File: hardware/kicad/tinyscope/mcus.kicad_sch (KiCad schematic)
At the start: 14 parts, among them U10 STM32H753VITx

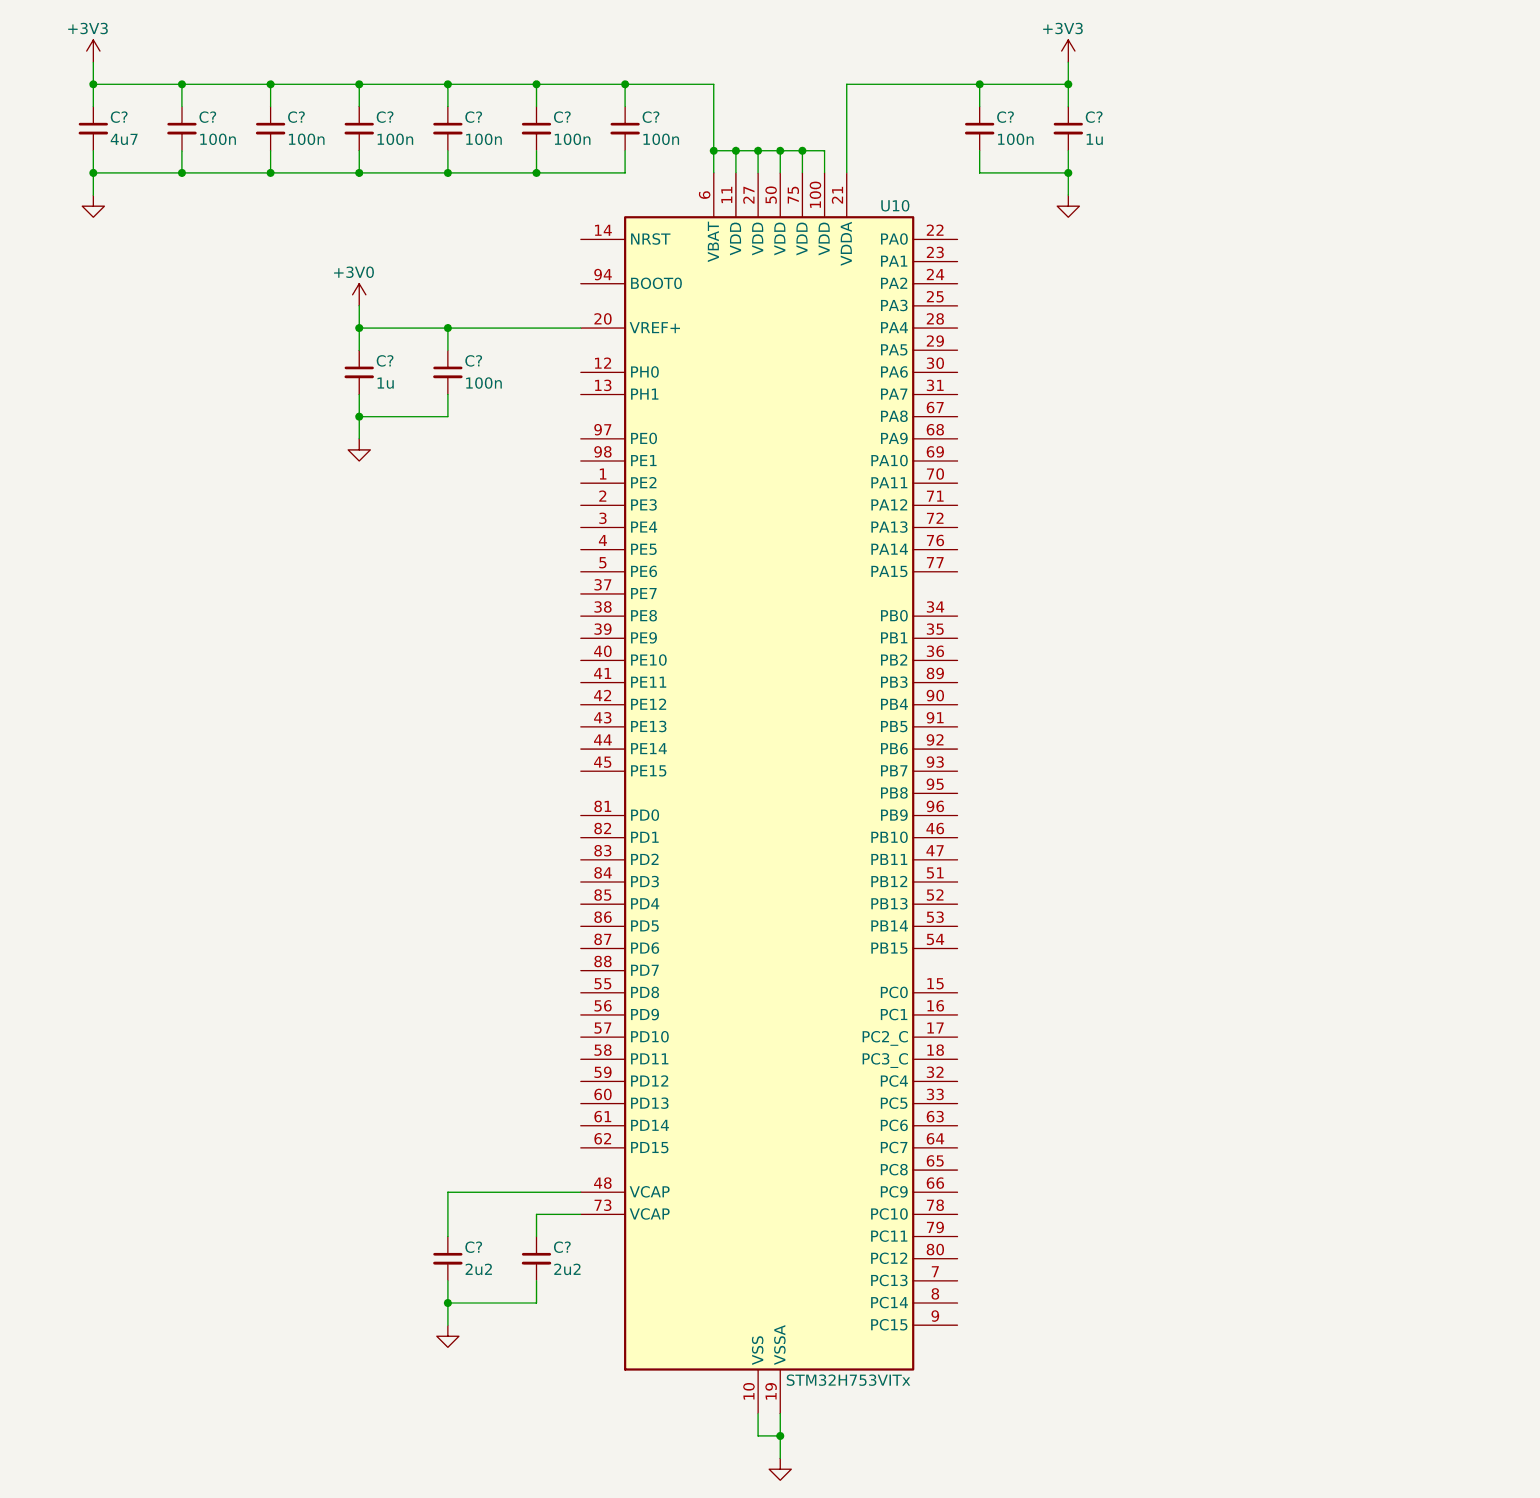
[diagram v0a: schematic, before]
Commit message: feat: hardware: Add tinyscope kicad project. Adds SWD NRST and BOOT0
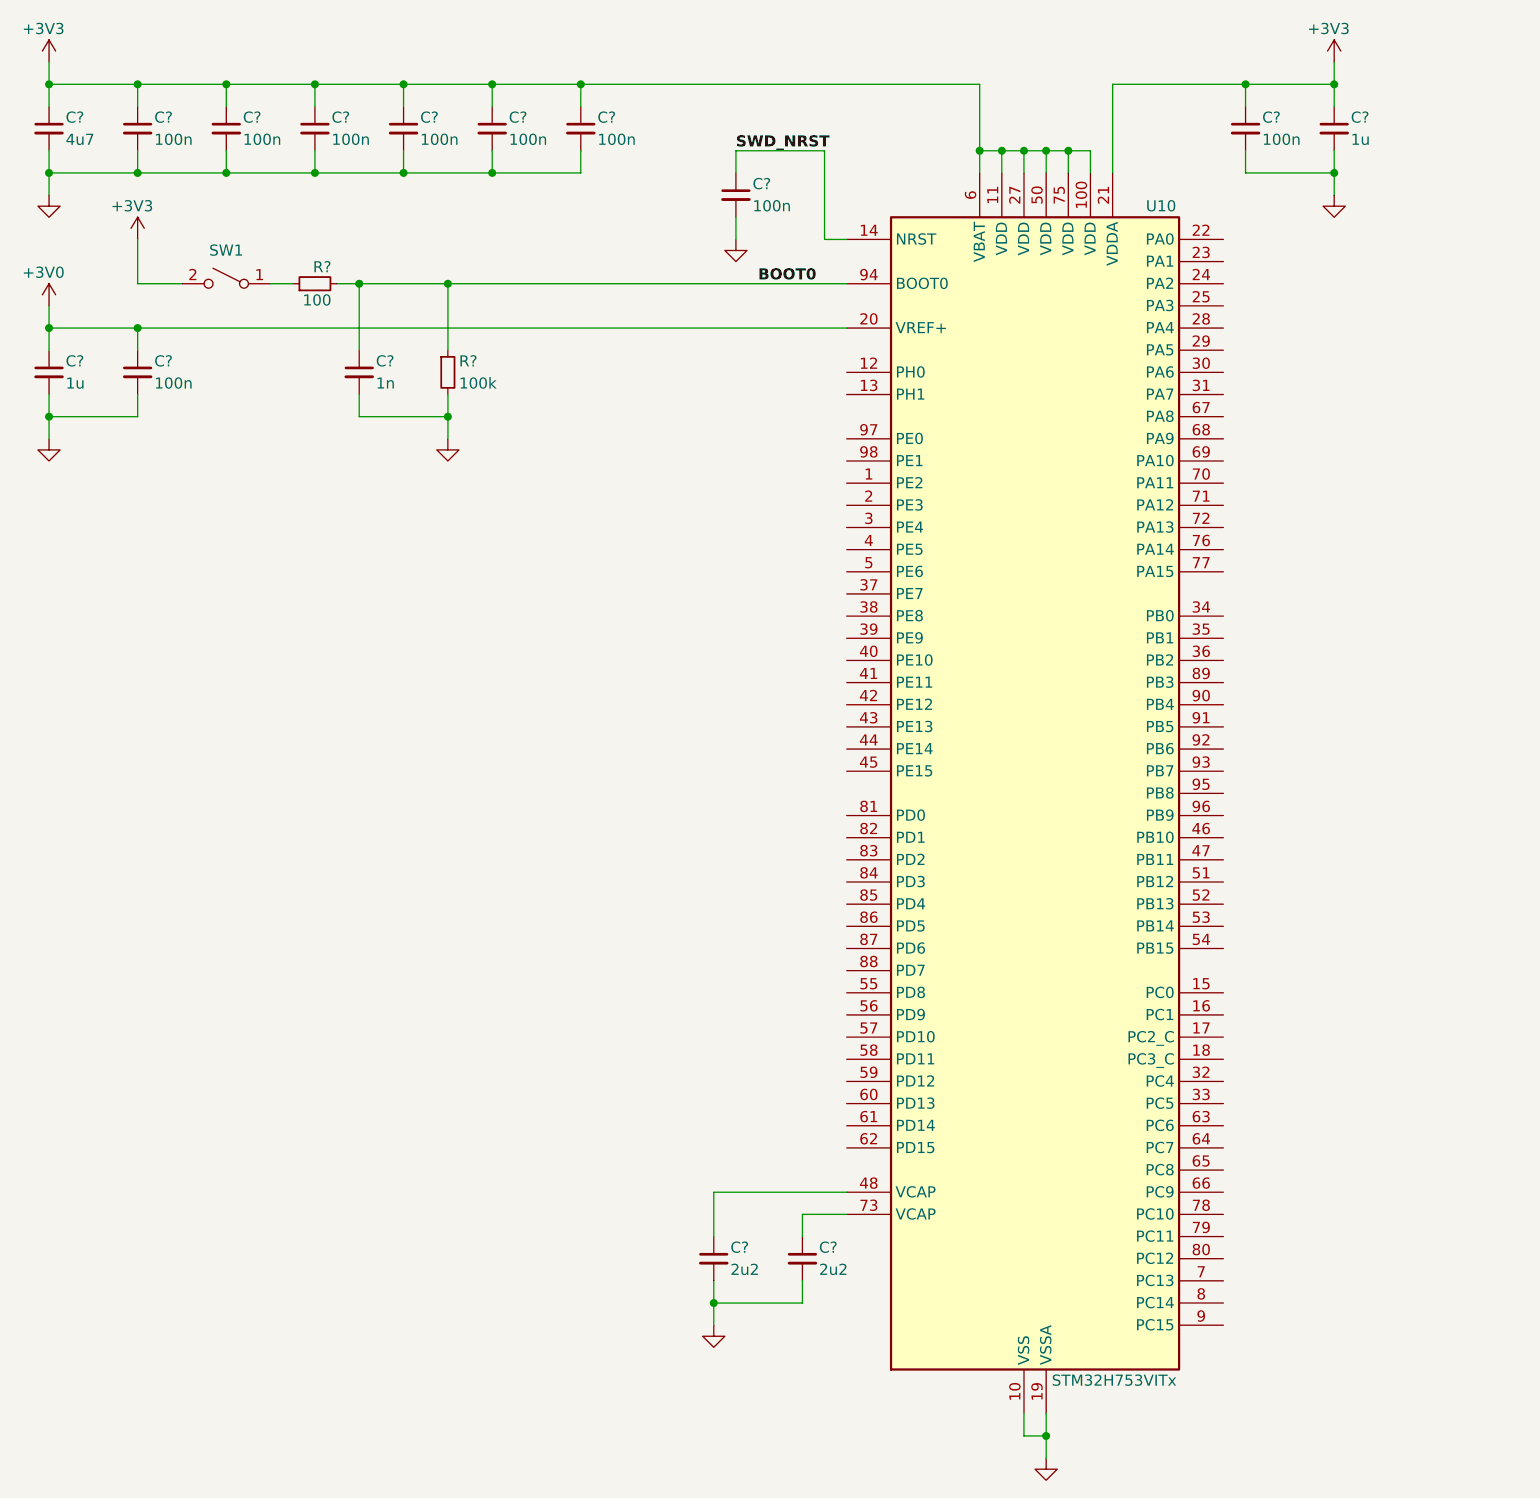
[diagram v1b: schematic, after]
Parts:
- added C?: 100n, symbol Device:C_Small
- added C?: 1n, symbol Device:C_Small
- added R?: 100k, symbol Device:R_Small
- added R?: 100, symbol Device:R_Small
- added SW1: SW_SPST, symbol Switch:SW_SPST
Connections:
- net +3V3: now also SW1.2 (B)
- net GND: now also C?.2, C?.2, R?.2
- net SWD_NRST: now reaches U10.14 (NRST)
- net SWD_NRST: now also C?.1
- net BOOT0: now reaches U10.94 (BOOT0)
- net BOOT0: now also C?.1, R?.1, R?.2
- new net: R?.1, SW1.1 (A)
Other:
- moved on the sheet: C?, U10

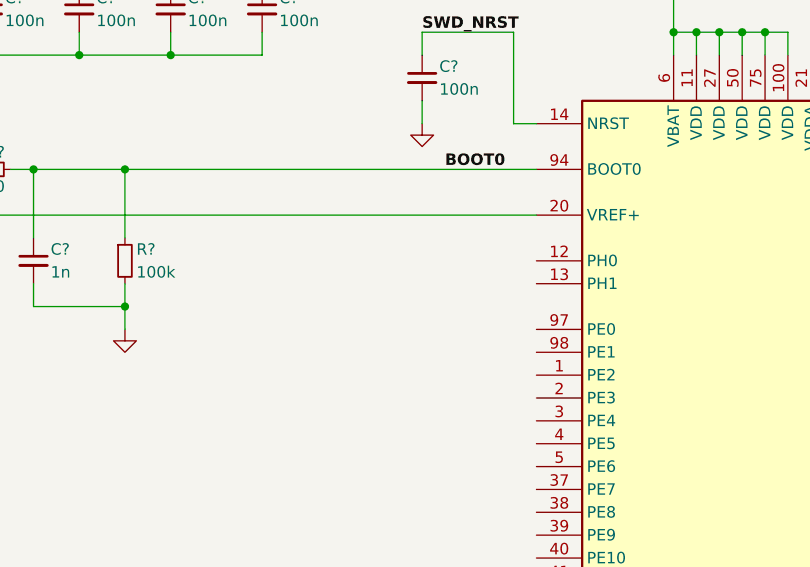
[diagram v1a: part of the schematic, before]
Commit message: feat: hardware: Add tinyscope kicad project. Adds HSE XTAL. Missing capacitor values
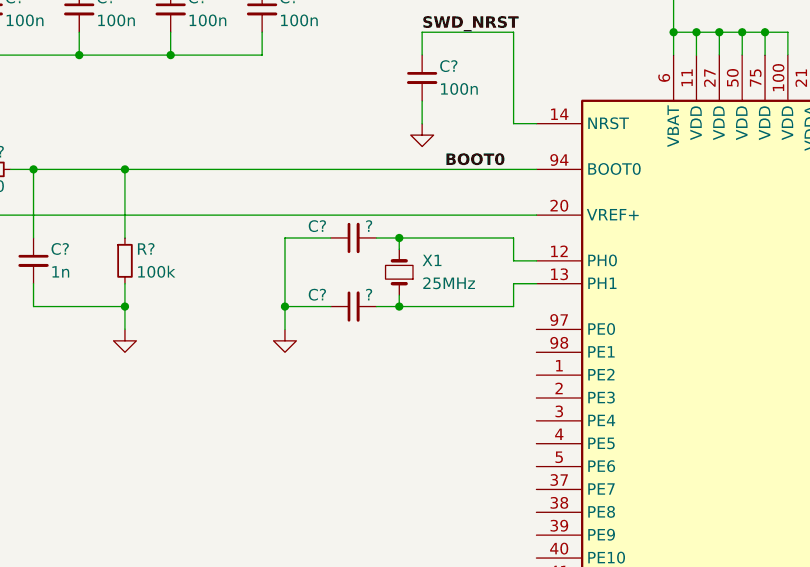
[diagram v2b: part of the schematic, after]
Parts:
- added C? (x2): ?, symbol Device:C_Small
- added X1: 25MHz, symbol Device:Crystal_Small
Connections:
- net GND: now also C?.1, C?.1
- net at U10.12 (PH0): now also C?.2, X1.2
- net at U10.13 (PH1): now also C?.2, X1.1
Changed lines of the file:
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@@
 (kicad_sch (version 20230121) (generator eeschema)
   (paper "A4")
+  (junction (at 96.52 60.96) (diameter 0) (color 0 0 0 0)
+  )
+  (junction (at 83.82 60.96) (diameter 0) (color 0 0 0 0)
+  )
   (junction (at 50.8 33.02) (diameter 0) (color 0 0 0 0)
   )
@@
   (junction (at 40.64 22.86) (diameter 0) (color 0 0 0 0)
   )
+  (junction (at 96.52 53.34) (diameter 0) (color 0 0 0 0)
+  )
   (junction (at 66.04 45.72) (diameter 0) (color 0 0 0 0)
   )
@@
     (stroke (width 0) (type default))
   )
+  (wire (pts (xy 109.22 58.42) (xy 109.22 60.96))
+    (stroke (width 0) (type default))
+  )
   (wire (pts (xy 167.64 33.02) (xy 167.64 35.56))
     (stroke (width 0) (type default))
@@
     (stroke (width 0) (type default))
   )
+  (wire (pts (xy 83.82 60.96) (xy 83.82 63.5))
+    (stroke (width 0) (type default))
+  )
   (wire (pts (xy 50.8 33.02) (xy 40.64 33.02))
     (stroke (width 0) (type default))
@@
     (stroke (width 0) (type default))
   )
+  (wire (pts (xy 111.76 55.88) (xy 109.22 55.88))
+    (stroke (width 0) (type default))
+  )
+  (wire (pts (xy 96.52 60.96) (xy 109.22 60.96))
+    (stroke (width 0) (type default))
+  )
   (wire (pts (xy 30.48 33.02) (xy 30.48 30.48))
     (stroke (width 0) (type default))
@@
     (stroke (width 0) (type default))
   )
+  (wire (pts (xy 109.22 55.88) (xy 109.22 53.34))
+    (stroke (width 0) (type default))
+  )
+  (wire (pts (xy 83.82 53.34) (xy 83.82 60.96))
+    (stroke (width 0) (type default))
+  )
   (wire (pts (xy 20.32 22.86) (xy 30.48 22.86))
     (stroke (width 0) (type default))
@@
     (stroke (width 0) (type default))
   )
+  (wire (pts (xy 93.98 60.96) (xy 96.52 60.96))
+    (stroke (width 0) (type default))
+  )
+  (wire (pts (xy 88.9 53.34) (xy 83.82 53.34))
+    (stroke (width 0) (type default))
+  )
   (wire (pts (xy 55.88 60.96) (xy 66.04 60.96))
     (stroke (width 0) (type default))
   )
+  (wire (pts (xy 93.98 53.34) (xy 96.52 53.34))
+    (stroke (width 0) (type default))
+  )
   (wire (pts (xy 127 30.48) (xy 127 22.86))
     (stroke (width 0) (type default))
@@
     (stroke (width 0) (type default))
   )
+  (wire (pts (xy 96.52 53.34) (xy 96.52 54.61))
+    (stroke (width 0) (type default))
+  )
   (wire (pts (xy 30.48 50.8) (xy 111.76 50.8))
     (stroke (width 0) (type default))
   )
+  (wire (pts (xy 111.76 58.42) (xy 109.22 58.42))
+    (stroke (width 0) (type default))
+  )
   (wire (pts (xy 96.52 162.56) (xy 106.68 162.56))
     (stroke (width 0) (type default))
@@
     (stroke (width 0) (type default))
   )
+  (wire (pts (xy 88.9 60.96) (xy 83.82 60.96))
+    (stroke (width 0) (type default))
+  )
   (wire (pts (xy 81.28 22.86) (xy 71.12 22.86))
     (stroke (width 0) (type default))
@@
     (stroke (width 0) (type default))
   )
+  (wire (pts (xy 96.52 53.34) (xy 109.22 53.34))
+    (stroke (width 0) (type default))
+  )
   (wire (pts (xy 129.54 33.02) (xy 129.54 30.48))
     (stroke (width 0) (type default))
   )
   (wire (pts (xy 81.28 22.86) (xy 81.28 25.4))
+    (stroke (width 0) (type default))
+  )
+  (wire (pts (xy 96.52 59.69) (xy 96.52 60.96))
     (stroke (width 0) (type default))
   )
@@
     )
   )
+  (symbol (lib_id "Device:C_Small") (at 91.44 53.34 90) (mirror x) (unit 1)
+    (in_bom yes) (on_board yes) (dnp no)
+    (property "Reference" "C?" (at 86.36 52.07 90)
+      (effects (font (size 1.27 1.27)) (justify right))
+    )
+    (property "Value" "?" (at 92.71 52.07 90)
+      (effects (font (size 1.27 1.27)) (justify right))
+    )
+    (property "Footprint" "" (at 91.44 53.34 0)
+      (effects (font (size 1.27 1.27)) hide)
+    )
+    (property "Datasheet" "~" (at 91.44 53.34 0)
+      (effects (font (size 1.27 1.27)) hide)
+    )
+    (pin "1")
+    (pin "2")
+    (instances
+      (project "tinyscope"
+        (path "/bb072e32-cc57-415a-8554-0e84d374f333"
+          (reference "C?") (unit 1)
+        )
+        (path "/bb072e32-cc57-415a-8554-0e84d374f333/7c1b1425-60eb-4f71-b125-42ba246f39fb"
+          (reference "C1") (unit 1)
+        )
+        (path "/bb072e32-cc57-415a-8554-0e84d374f333/f3c865ab-23cb-49a1-bb6d-4ee24e55c7fa"
+          (reference "C42") (unit 1)
+        )
+      )
+    )
+  )
   (symbol (lib_id "Device:C_Small") (at 71.12 27.94 0) (mirror y) (unit 1)
     (in_bom yes) (on_board yes) (dnp no)
@@
         (path "/bb072e32-cc57-415a-8554-0e84d374f333/f3c865ab-23cb-49a1-bb6d-4ee24e55c7fa"
           (reference "C27") (unit 1)
+        )
+      )
+    )
+  )
+  (symbol (lib_id "Device:Crystal_Small") (at 96.52 57.15 90) (unit 1)
+    (in_bom yes) (on_board yes) (dnp no) (fields_autoplaced)
+    (property "Reference" "X1" (at 99.06 55.88 90)
+      (effects (font (size 1.27 1.27)) (justify right))
+    )
+    (property "Value" "25MHz" (at 99.06 58.42 90)
+      (effects (font (size 1.27 1.27)) (justify right))
+    )
+    (property "Footprint" "" (at 96.52 57.15 0)
+      (effects (font (size 1.27 1.27)) hide)
+    )
+    (property "Datasheet" "~" (at 96.52 57.15 0)
+      (effects (font (size 1.27 1.27)) hide)
+    )
+    (pin "1")
+    (pin "2")
+    (instances
+      (project "tinyscope"
+        (path "/bb072e32-cc57-415a-8554-0e84d374f333/f3c865ab-23cb-49a1-bb6d-4ee24e55c7fa"
+          (reference "X1") (unit 1)
         )
       )
@@
         (path "/bb072e32-cc57-415a-8554-0e84d374f333/f3c865ab-23cb-49a1-bb6d-4ee24e55c7fa"
           (reference "C35") (unit 1)
+        )
+      )
+    )
+  )
+  (symbol (lib_id "Device:C_Small") (at 91.44 60.96 90) (mirror x) (unit 1)
+    (in_bom yes) (on_board yes) (dnp no)
+    (property "Reference" "C?" (at 86.36 59.69 90)
+      (effects (font (size 1.27 1.27)) (justify right))
+    )
+    (property "Value" "?" (at 92.71 59.69 90)
+      (effects (font (size 1.27 1.27)) (justify right))
+    )
+    (property "Footprint" "" (at 91.44 60.96 0)
+      (effects (font (size 1.27 1.27)) hide)
+    )
+    (property "Datasheet" "~" (at 91.44 60.96 0)
+      (effects (font (size 1.27 1.27)) hide)
+    )
+    (pin "1")
+    (pin "2")
+    (instances
+      (project "tinyscope"
+        (path "/bb072e32-cc57-415a-8554-0e84d374f333"
+          (reference "C?") (unit 1)
+        )
+        (path "/bb072e32-cc57-415a-8554-0e84d374f333/7c1b1425-60eb-4f71-b125-42ba246f39fb"
+          (reference "C1") (unit 1)
+        )
+        (path "/bb072e32-cc57-415a-8554-0e84d374f333/f3c865ab-23cb-49a1-bb6d-4ee24e55c7fa"
+          (reference "C41") (unit 1)
         )
       )
@@
         )
       )
+    )
+  )
+  (symbol (lib_id "power:GND") (at 83.82 63.5 0) (mirror y) (unit 1)
+    (in_bom yes) (on_board yes) (dnp no) (fields_autoplaced)
+    (property "Reference" "#PWR?" (at 83.82 69.85 0)
+      (effects (font (size 1.27 1.27)) hide)
+    )
+    (property "Value" "GND" (at 83.82 68.58 0)
+      (effects (font (size 1.27 1.27)) hide)
+    )
+    (property "Footprint" "" (at 83.82 63.5 0)
+      (effects (font (size 1.27 1.27)) hide)
+    )
+    (property "Datasheet" "" (at 83.82 63.5 0)
+      (effects (font (size 1.27 1.27)) hide)
+    )
+    (pin "1")
+    (instances
+      (project "tinyscope"
+        (path "/bb072e32-cc57-415a-8554-0e84d374f333"
+          (reference "#PWR?") (unit 1)
+        )
+        (path "/bb072e32-cc57-415a-8554-0e84d374f333/1c26ba79-0794-42b8-82e1-265696d83365"
+          (reference "#PWR034") (unit 1)
+        )
+        (path "/bb072e32-cc57-415a-8554-0e84d374f333/f3c865ab-23cb-49a1-bb6d-4ee24e55c7fa"
+          (reference "#PWR052") (unit 1)
+        )
+      )
